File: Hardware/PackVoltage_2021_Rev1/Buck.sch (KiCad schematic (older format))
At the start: 24 parts, among them J12V1 Test_Point, J3V1 Test_Point, J5V1 Test_Point, U10 LM2576S-12/NOPB, U11 LM2576SX-5.0/NOPB, U12 LM2576SX-3.3/NOPB

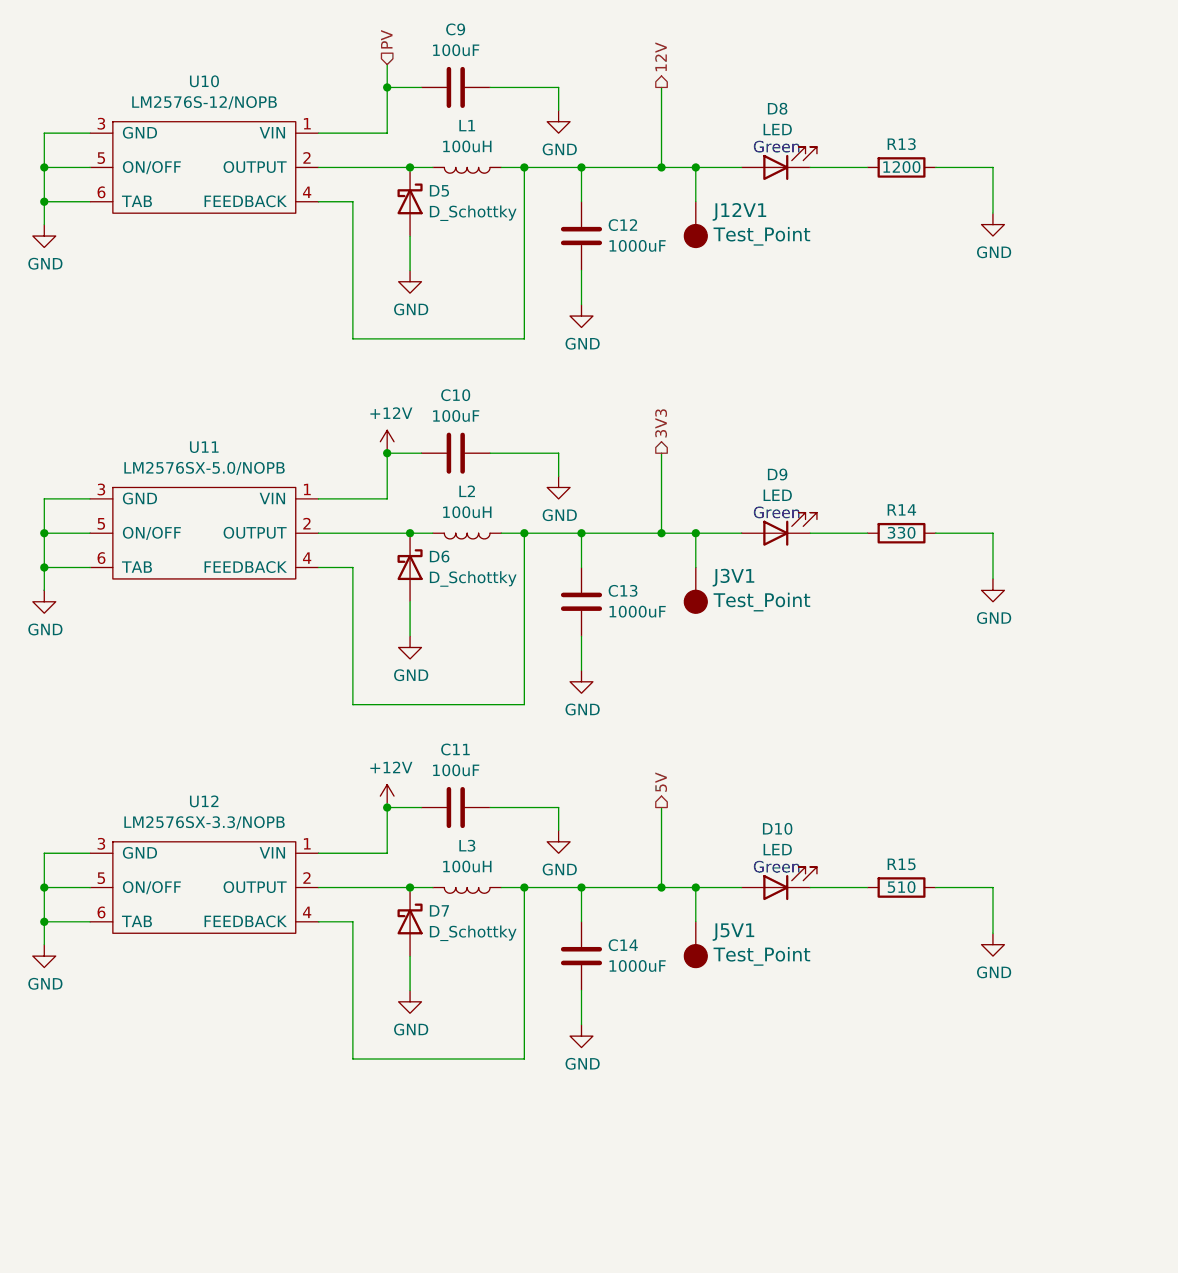
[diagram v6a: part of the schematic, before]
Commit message: Rearranged Bucks and Fixed 12V Bus LED Resistor
Moved 5v bus to the middle and 3.3V bus to the bottom to make things more clear.
12 bus had 3300 ohm resistor when it should have 1200 ohm b/c it only has 12 V going into it
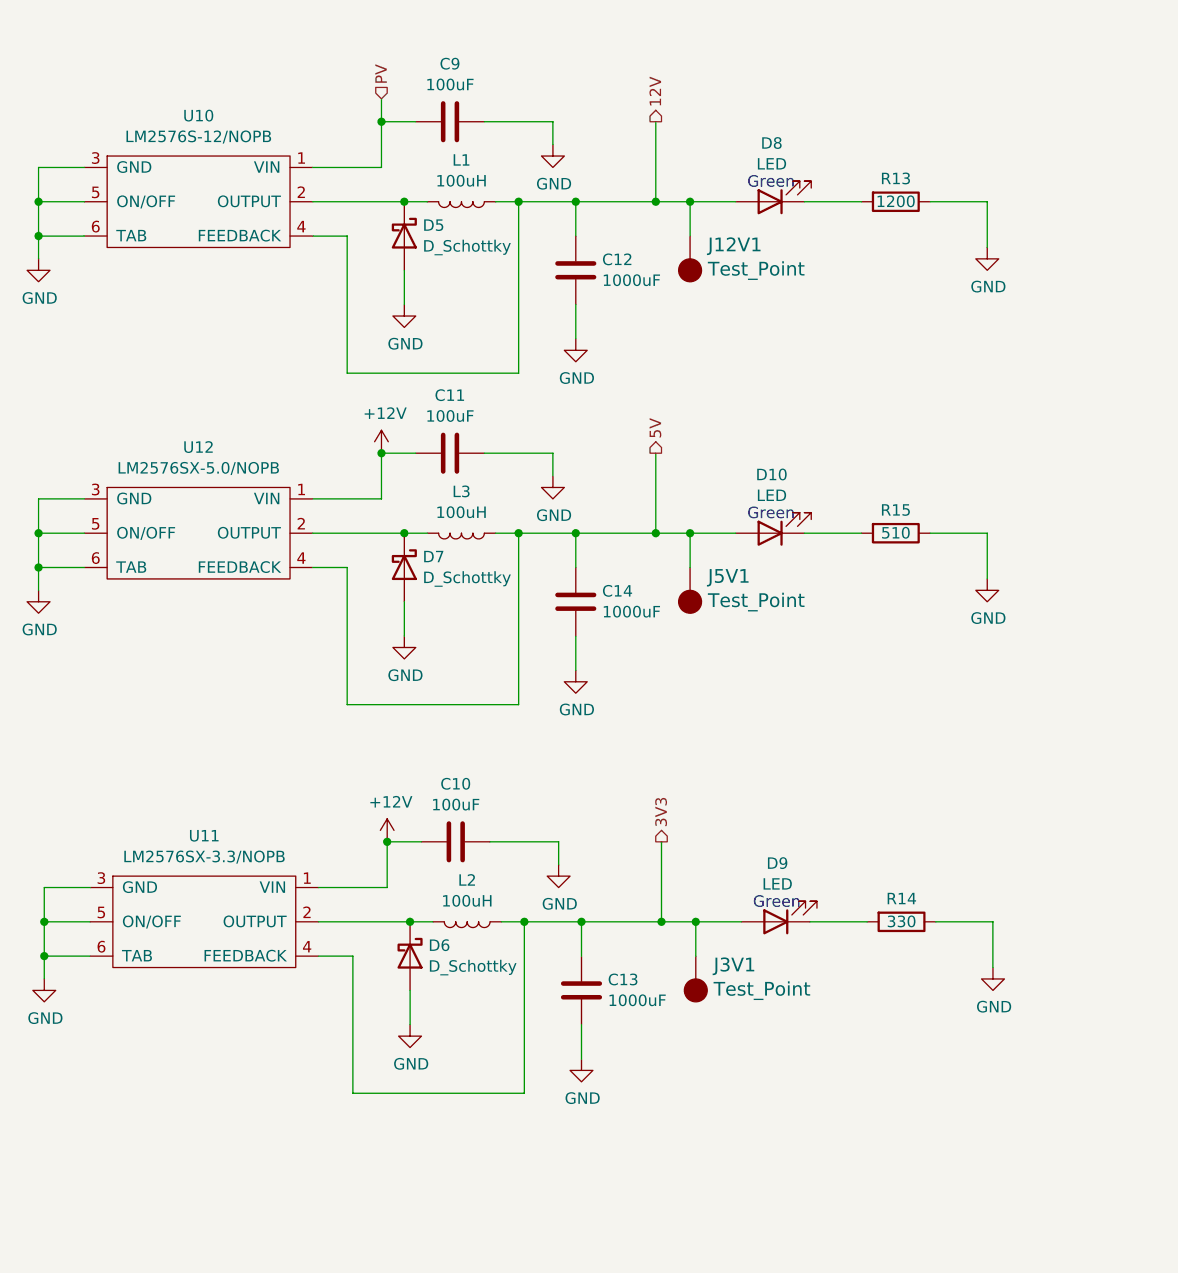
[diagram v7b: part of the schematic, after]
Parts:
- U11: value LM2576SX-5.0/NOPB -> LM2576SX-3.3/NOPB
- U12: value LM2576SX-3.3/NOPB -> LM2576SX-5.0/NOPB
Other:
- moved on the sheet: C10, C11, C12, C13, C14, C9, D10, D5, D6, D7, D8, D9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

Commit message: Added GimbalSense, reannotated
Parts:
- renumbered C9 to C15, C11 to C16, C10 to C17, C12 to C18, C14 to C19, C13 to C20, D6 to D10, D8 to D11, D10 to D12, D9 to D13, D5 to D8, D7 to D9, L3 to L2, L2 to L3, R13 to R16, R15 to R17, R14 to R18, U10 to U11, U11 to U13
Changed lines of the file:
@@
 $EndComp
 $Comp
-L power:GND #PWR030
+L power:GND #PWR032
 U 1 1 5F86AD77
 P 875 3200
-F 0 "#PWR030" H 875 2950 50  0001 C CNN
+F 0 "#PWR032" H 875 2950 50  0001 C CNN
 F 1 "GND" H 880 3027 50  0000 C CNN
 F 2 "" H 875 3200 50  0001 C CNN
@@
 	2075 2800 2375 2800
 $Comp
-L Device:C C11
+L Device:C C16
 U 1 1 5F86AD86
 P 2675 2600
-F 0 "C11" V 2423 2600 50  0000 C CNN
+F 0 "C16" V 2423 2600 50  0000 C CNN
 F 1 "100uF" V 2514 2600 50  0000 C CNN
 F 2 "" H 2713 2450 50  0001 C CNN
@@
 	2375 2600 2525 2600
 $Comp
-L power:GND #PWR038
+L power:GND #PWR040
 U 1 1 5F86AD8D
 P 3125 2700
-F 0 "#PWR038" H 3125 2450 50  0001 C CNN
+F 0 "#PWR040" H 3125 2450 50  0001 C CNN
 F 1 "GND" H 3130 2527 50  0000 C CNN
 F 2 "" H 3125 2700 50  0001 C CNN
@@
 	3125 2600 3125 2700
 $Comp
-L Device:D_Schottky D7
+L Device:D_Schottky D9
 U 1 1 5F86AD98
 P 2475 3100
-F 0 "D7" V 2429 3180 50  0000 L CNN
+F 0 "D9" V 2429 3180 50  0000 L CNN
 F 1 "D_Schottky" V 2520 3180 50  0000 L CNN
 F 2 "" H 2475 3100 50  0001 C CNN
@@
 	2075 2950 2475 2950
 $Comp
-L Device:L L3
+L Device:L L2
 U 1 1 5F86AD9F
 P 2725 2950
-F 0 "L3" V 2544 2950 50  0000 C CNN
+F 0 "L2" V 2544 2950 50  0000 C CNN
 F 1 "100uH" V 2635 2950 50  0000 C CNN
 F 2 "" H 2725 2950 50  0001 C CNN
@@
 Connection ~ 2475 2950
 $Comp
-L power:GND #PWR035
+L power:GND #PWR037
 U 1 1 5F86ADA7
 P 2475 3400
-F 0 "#PWR035" H 2475 3150 50  0001 C CNN
+F 0 "#PWR037" H 2475 3150 50  0001 C CNN
 F 1 "GND" H 2480 3227 50  0000 C CNN
 F 2 "" H 2475 3400 50  0001 C CNN
@@
 Connection ~ 2975 2950
 $Comp
-L Device:C C14
+L Device:C C19
 U 1 1 5F86ADB5
 P 3225 3250
-F 0 "C14" H 3340 3296 50  0000 L CNN
+F 0 "C19" H 3340 3296 50  0000 L CNN
 F 1 "1000uF" H 3340 3205 50  0000 L CNN
 F 2 "" H 3263 3100 50  0001 C CNN
@@
 	3225 2950 3225 3100
 $Comp
-L power:GND #PWR041
+L power:GND #PWR043
 U 1 1 5F86ADBC
 P 3225 3550
-F 0 "#PWR041" H 3225 3300 50  0001 C CNN
+F 0 "#PWR043" H 3225 3300 50  0001 C CNN
 F 1 "GND" H 3230 3377 50  0000 C CNN
 F 2 "" H 3225 3550 50  0001 C CNN
@@
 Connection ~ 3575 2950
 $Comp
-L Device:LED D10
+L Device:LED D12
 U 1 1 5F86ADD5
 P 4075 2950
-F 0 "D10" H 4068 2695 50  0000 C CNN
+F 0 "D12" H 4068 2695 50  0000 C CNN
 F 1 "LED" H 4068 2786 50  0000 C CNN
 F 2 "" H 4075 2950 50  0001 C CNN
@@
 $EndComp
 $Comp
-L Device:R R15
+L Device:R R17
 U 1 1 5F86ADDB
 P 4625 2950
-F 0 "R15" V 4525 2950 50  0000 C CNN
+F 0 "R17" V 4525 2950 50  0000 C CNN
 F 1 "510" V 4625 2950 50  0000 C CNN
 F 2 "" V 4555 2950 50  0001 C CNN
@@
 $EndComp
 $Comp
-L power:GND #PWR047
+L power:GND #PWR046
 U 1 1 5F86ADE1
 P 5025 3150
-F 0 "#PWR047" H 5025 2900 50  0001 C CNN
+F 0 "#PWR046" H 5025 2900 50  0001 C CNN
 F 1 "GND" H 5030 2977 50  0000 C CNN
 F 2 "" H 5025 3150 50  0001 C CNN
@@
 	2375 2600 2375 2800
 $Comp
-L power:+12V #PWR032
+L power:+12V #PWR034
 U 1 1 5F8711D0
 P 2375 2600
-F 0 "#PWR032" H 2375 2450 50  0001 C CNN
+F 0 "#PWR034" H 2375 2450 50  0001 C CNN
 F 1 "+12V" H 2390 2773 50  0000 C CNN
 F 2 "" H 2375 2600 50  0001 C CNN
@@
 $EndComp
 $Comp
-L MRDT_Devices:LM2576D2TR4 U11
+L MRDT_Devices:LM2576D2TR4 U13
 U 1 1 5F874FF1
 P 1600 4700
-F 0 "U11" H 1600 5125 50  0000 C CNN
+F 0 "U13" H 1600 5125 50  0000 C CNN
 F 1 "LM2576SX-3.3/NOPB" H 1600 5034 50  0000 C CNN
 F 2 "" H 1600 5150 50  0001 C CNN
@@
 $EndComp
 $Comp
-L power:GND #PWR029
+L power:GND #PWR033
 U 1 1 5F874FF7
 P 900 4900
-F 0 "#PWR029" H 900 4650 50  0001 C CNN
+F 0 "#PWR033" H 900 4650 50  0001 C CNN
 F 1 "GND" H 905 4727 50  0000 C CNN
 F 2 "" H 900 4900 50  0001 C CNN
@@
 	2100 4500 2400 4500
 $Comp
-L Device:C C10
+L Device:C C17
 U 1 1 5F875006
 P 2700 4300
-F 0 "C10" V 2448 4300 50  0000 C CNN
+F 0 "C17" V 2448 4300 50  0000 C CNN
 F 1 "100uF" V 2539 4300 50  0000 C CNN
 F 2 "" H 2738 4150 50  0001 C CNN
@@
 	2400 4300 2550 4300
 $Comp
-L power:GND #PWR037
+L power:GND #PWR041
 U 1 1 5F87500D
 P 3150 4400
-F 0 "#PWR037" H 3150 4150 50  0001 C CNN
+F 0 "#PWR041" H 3150 4150 50  0001 C CNN
 F 1 "GND" H 3155 4227 50  0000 C CNN
 F 2 "" H 3150 4400 50  0001 C CNN
@@
 	3150 4300 3150 4400
 $Comp
-L Device:D_Schottky D6
+L Device:D_Schottky D10
 U 1 1 5F875015
 P 2500 4800
-F 0 "D6" V 2454 4880 50  0000 L CNN
+F 0 "D10" V 2454 4880 50  0000 L CNN
 F 1 "D_Schottky" V 2545 4880 50  0000 L CNN
 F 2 "" H 2500 4800 50  0001 C CNN
@@
 	2100 4650 2500 4650
 $Comp
-L Device:L L2
+L Device:L L3
 U 1 1 5F87501C
 P 2750 4650
-F 0 "L2" V 2569 4650 50  0000 C CNN
+F 0 "L3" V 2569 4650 50  0000 C CNN
 F 1 "100uH" V 2660 4650 50  0000 C CNN
 F 2 "" H 2750 4650 50  0001 C CNN
@@
 Connection ~ 2500 4650
 $Comp
-L power:GND #PWR034
+L power:GND #PWR038
 U 1 1 5F875024
 P 2500 5100
-F 0 "#PWR034" H 2500 4850 50  0001 C CNN
+F 0 "#PWR038" H 2500 4850 50  0001 C CNN
 F 1 "GND" H 2505 4927 50  0000 C CNN
 F 2 "" H 2500 5100 50  0001 C CNN
@@
 Connection ~ 3000 4650
 $Comp
-L Device:C C13
+L Device:C C20
 U 1 1 5F875032
 P 3250 4950
-F 0 "C13" H 3365 4996 50  0000 L CNN
+F 0 "C20" H 3365 4996 50  0000 L CNN
 F 1 "1000uF" H 3365 4905 50  0000 L CNN
 F 2 "" H 3288 4800 50  0001 C CNN
@@
 	3250 4650 3250 4800
 $Comp
-L power:GND #PWR040
+L power:GND #PWR044
 U 1 1 5F875039
 P 3250 5250
-F 0 "#PWR040" H 3250 5000 50  0001 C CNN
+F 0 "#PWR044" H 3250 5000 50  0001 C CNN
 F 1 "GND" H 3255 5077 50  0000 C CNN
 F 2 "" H 3250 5250 50  0001 C CNN
@@
 Connection ~ 3600 4650
 $Comp
-L Device:LED D9
+L Device:LED D13
 U 1 1 5F87504C
 P 4100 4650
-F 0 "D9" H 4093 4395 50  0000 C CNN
+F 0 "D13" H 4093 4395 50  0000 C CNN
 F 1 "LED" H 4093 4486 50  0000 C CNN
 F 2 "" H 4100 4650 50  0001 C CNN
@@
 $EndComp
 $Comp
-L Device:R R14
+L Device:R R18
 U 1 1 5F875052
 P 4650 4650
-F 0 "R14" V 4550 4650 50  0000 C CNN
+F 0 "R18" V 4550 4650 50  0000 C CNN
 F 1 "330" V 4650 4650 50  0000 C CNN
 F 2 "" V 4580 4650 50  0001 C CNN
@@
 $EndComp
 $Comp
-L power:GND #PWR046
+L power:GND #PWR047
 U 1 1 5F875058
 P 5050 4850
-F 0 "#PWR046" H 5050 4600 50  0001 C CNN
+F 0 "#PWR047" H 5050 4600 50  0001 C CNN
 F 1 "GND" H 5055 4677 50  0000 C CNN
 F 2 "" H 5050 4850 50  0001 C CNN
@@
 	2400 4300 2400 4500
 $Comp
-L power:+12V #PWR031
+L power:+12V #PWR035
 U 1 1 5F875065
 P 2400 4300
-F 0 "#PWR031" H 2400 4150 50  0001 C CNN
+F 0 "#PWR035" H 2400 4150 50  0001 C CNN
 F 1 "+12V" H 2415 4473 50  0000 C CNN
 F 2 "" H 2400 4300 50  0001 C CNN
@@
 3V3
 $Comp
-L MRDT_Devices:LM2576D2TR4 U10
+L MRDT_Devices:LM2576D2TR4 U11
 U 1 1 5F826D23
 P 1575 1550
-F 0 "U10" H 1575 1975 50  0000 C CNN
+F 0 "U11" H 1575 1975 50  0000 C CNN
 F 1 "LM2576S-12/NOPB" H 1575 1884 50  0000 C CNN
 F 2 "" H 1575 2000 50  0001 C CNN
@@
 $EndComp
 $Comp
-L Device:R R13
+L Device:R R16
 U 1 1 5F8316D9
 P 4625 1500
-F 0 "R13" V 4525 1500 50  0000 C CNN
+F 0 "R16" V 4525 1500 50  0000 C CNN
 F 1 "1200" V 4625 1500 50  0000 C CNN
 F 2 "" V 4555 1500 50  0001 C CNN
@@
 $EndComp
 $Comp
-L Device:LED D8
+L Device:LED D11
 U 1 1 5F83034C
 P 4075 1500
-F 0 "D8" H 4068 1245 50  0000 C CNN
+F 0 "D11" H 4068 1245 50  0000 C CNN
 F 1 "LED" H 4068 1336 50  0000 C CNN
 F 2 "" H 4075 1500 50  0001 C CNN
@@
 	3225 1950 3225 2100
 $Comp
-L power:GND #PWR039
+L power:GND #PWR042
 U 1 1 5F82E079
 P 3225 2100
-F 0 "#PWR039" H 3225 1850 50  0001 C CNN
+F 0 "#PWR042" H 3225 1850 50  0001 C CNN
 F 1 "GND" H 3230 1927 50  0000 C CNN
 F 2 "" H 3225 2100 50  0001 C CNN
@@
 	3225 1500 3225 1650
 $Comp
-L Device:C C12
+L Device:C C18
 U 1 1 5F82D7D6
 P 3225 1800
-F 0 "C12" H 3340 1846 50  0000 L CNN
+F 0 "C18" H 3340 1846 50  0000 L CNN
 F 1 "1000uF" H 3340 1755 50  0000 L CNN
 F 2 "" H 3263 1650 50  0001 C CNN
@@
 	2475 1800 2475 1950
 $Comp
-L power:GND #PWR033
+L power:GND #PWR036
 U 1 1 5F82BB1D
 P 2475 1950
-F 0 "#PWR033" H 2475 1700 50  0001 C CNN
+F 0 "#PWR036" H 2475 1700 50  0001 C CNN
 F 1 "GND" H 2480 1777 50  0000 C CNN
 F 2 "" H 2475 1950 50  0001 C CNN
@@
 	2075 1500 2475 1500
 $Comp
-L Device:D_Schottky D5
+L Device:D_Schottky D8
 U 1 1 5F82A21A
 P 2475 1650
-F 0 "D5" V 2429 1730 50  0000 L CNN
+F 0 "D8" V 2429 1730 50  0000 L CNN
 F 1 "D_Schottky" V 2520 1730 50  0000 L CNN
 F 2 "" H 2475 1650 50  0001 C CNN
@@
 	2825 1150 3125 1150
 $Comp
-L power:GND #PWR036
+L power:GND #PWR039
 U 1 1 5F828A9F
 P 3125 1250
-F 0 "#PWR036" H 3125 1000 50  0001 C CNN
+F 0 "#PWR039" H 3125 1000 50  0001 C CNN
 F 1 "GND" H 3130 1077 50  0000 C CNN
 F 2 "" H 3125 1250 50  0001 C CNN
@@
 	2375 1150 2525 1150
 $Comp
-L Device:C C9
+L Device:C C15
 U 1 1 5F828247
 P 2675 1150
-F 0 "C9" V 2423 1150 50  0000 C CNN
+F 0 "C15" V 2423 1150 50  0000 C CNN
 F 1 "100uF" V 2514 1150 50  0000 C CNN
 F 2 "" H 2713 1000 50  0001 C CNN
@@
 	1075 1350 875  1350
 $Comp
-L power:GND #PWR028
+L power:GND #PWR031
 U 1 1 5F827523
 P 875 1750
-F 0 "#PWR028" H 875 1500 50  0001 C CNN
+F 0 "#PWR031" H 875 1500 50  0001 C CNN
 F 1 "GND" H 880 1577 50  0000 C CNN
 F 2 "" H 875 1750 50  0001 C CNN
